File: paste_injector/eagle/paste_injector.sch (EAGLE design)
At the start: 20 parts, among them IC1 ULN2003AD, J2 USB, J5 PINHD-2X3, Q2 CSTCR6M00G53Z, U2 FT232RL, U4 ATMEGA328TQFP32

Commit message: Work in progress.
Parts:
- removed C5, C6, C7: 0.1uF, paste_injector:CAP-C0603
- removed U$28: OSH, paste_injector:OSH
- removed U2: FT232RL, paste_injector:FT232RL
- added C1: 0.1uF, paste_injector:CAP-C0603
- added JP2: (no value), paste_injector:PINHD-1X6
- R10, R2: value 10K -> 5K
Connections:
- removed net N$11: C6.1, U2.DTRO
- removed net N$16: C7.1, U2.3V3OUT
- removed net SER_RX: U2.TXO, U4.PD0(RXD)
- removed net SER_TX: U2.RXI, U4.PD1(TXD)
- removed net USB_DM: J2.D-, U2.D-
- removed net USB_DP: J2.D+, U2.D+
- new net DTR: C1.2, JP2.6
- new net RXI: JP2.4, U4.PD0(RXD)
- new net TXO: JP2.5, U4.PD1(TXD)
- net +5V: now also JP2.3; no longer C5.1, U2.VCC, U2.VCCIO
- net GND: now also JP2.1, JP2.2; no longer C5.2, C7.2, U2.GND@1, U2.GND@2, U2.GND@3, U2.GND@4, U2.TEST
- net RESET: now also C1.1; no longer C6.2
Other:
- note added: "0"
- note added: "FTDI BASIC"
- note added: "STATUS: EARLY DRAFT, DESIGN NOT VERIFIED YET."
- note removed: "1"
- note removed: "Serial (optional for debugging)"
- note removed: "TODO: add leds"
- moved on the sheet: C3, IC1, J5, JP1

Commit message: Minor tweaks.
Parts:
- removed JP2: (no value), paste_injector:PINHD-1X6
- removed LED1: (no value), arm-pro-mini-tester:LED
- added D1: (no value), paste_injector:LED
- added J1: USB, paste_injector:USB
- C1: value 0.1uF -> 10uF; device paste_injector:CAP-C0603 -> paste_injector:CPOL-USA/3216-18R
- C3: value 10uF -> 0.1uF; device paste_injector:CPOL-USA/3216-18R -> paste_injector:CAP-C0603
- J2: value USB -> (none); device paste_injector:USB -> paste_injector:PINHD-1X6
- R1: value (none) -> 10K; device paste_injector:TRIM_US-CA9V -> paste_injector:TRIMPOTCA9V
- renumbered C10 to C4, IC1 to U2, J5 to ISP, JP1 to J3, Q2 to Q1, R10 to R3, U4 to U1
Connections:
- net +5V: now also C1.+, J1.VBUS, J2.3, R1.CW; no longer C3.+, J2.VBUS, JP2.3, R1.E
- net BACKWARD: now also S2.2; no longer S1.2
- net DTR: now also C3.2, J2.6; no longer C1.2, JP2.6
- net FORWARD: now also S1.2; no longer S2.2
- net GND: now also C1.-, D1.C, J1.GND, J2.1, J2.2, R1.CCW, S1.GND, S2.GND; no longer C3.-, J2.GND, JP2.1, JP2.2, LED1.C, R1.A
- net M1: now also U1.PD2(INT0); no longer U1.PC2(ADC2)
- net M2: now also U1.PD3(INT1); no longer U1.PC3(ADC3)
- net M3: now also U1.PD4(XCK/T0); no longer U1.ADC6
- net M4: now also U1.PD5(T1); no longer U1.ADC7
- net N$1: now also D1.A; no longer LED1.A
- net POT: now also R1.C; no longer R1.S
- net RESET: now also C3.1; no longer C1.1
- net RXI: now also J2.4; no longer JP2.4
- net TXO: now also J2.5; no longer JP2.5
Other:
- note added: "+5V"
- note added: "CTS"
- note added: "DTR"
- note added: "GND"
- note added: "RXI"
- note added: "STATUS: NON VERIFIED DRAFT."
- note added: "TXO"
- note removed: "STATUS: EARLY DRAFT, DESIGN NOT VERIFIED YET."
- note removed: "TODO: pick potentiometer"
- note removed: "TODO: pick push buttons"
- moved on the sheet: C2

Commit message: Performed final routing.
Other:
- note added: "PUSH SPEED"
- note removed: "SPEED"
- moved on the sheet: J1
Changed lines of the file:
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@@
 <text x="172.72" y="68.58" size="3.048" layer="97">ISP</text>
 <text x="2.54" y="154.94" size="3.048" layer="97">POWER</text>
-<text x="15.24" y="96.52" size="3.048" layer="97">SPEED</text>
+<text x="15.24" y="96.52" size="3.048" layer="97">PUSH SPEED</text>
 <text x="96.52" y="71.12" size="3.048" layer="97">MOTOR DRIVER</text>
 <text x="200.66" y="116.84" size="3.048" layer="97">MCU</text>

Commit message: Saving open files.
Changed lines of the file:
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@@
 <part name="U$7" library="paste_injector" deviceset="NC" device=""/>
 <part name="R1" library="paste_injector" deviceset="TRIMPOT" device="CA9V" value="10K"/>
+<part name="U$8" library="paste_injector" deviceset="NC" device=""/>
+<part name="U$10" library="paste_injector" deviceset="NC" device=""/>
+<part name="U$11" library="paste_injector" deviceset="NC" device=""/>
+<part name="U$12" library="paste_injector" deviceset="NC" device=""/>
 </parts>
 <sheets>
@@
 <instance part="U$7" gate="G$1" x="231.14" y="177.8" rot="R180"/>
 <instance part="R1" gate="G$1" x="2.54" y="111.76"/>
+<instance part="U$8" gate="G$1" x="182.88" y="182.88" rot="R180"/>
+<instance part="U$10" gate="G$1" x="106.68" y="104.14" rot="R180"/>
+<instance part="U$11" gate="G$1" x="106.68" y="101.6" rot="R180"/>
+<instance part="U$12" gate="G$1" x="106.68" y="99.06" rot="R180"/>
 </instances>
 <busses>

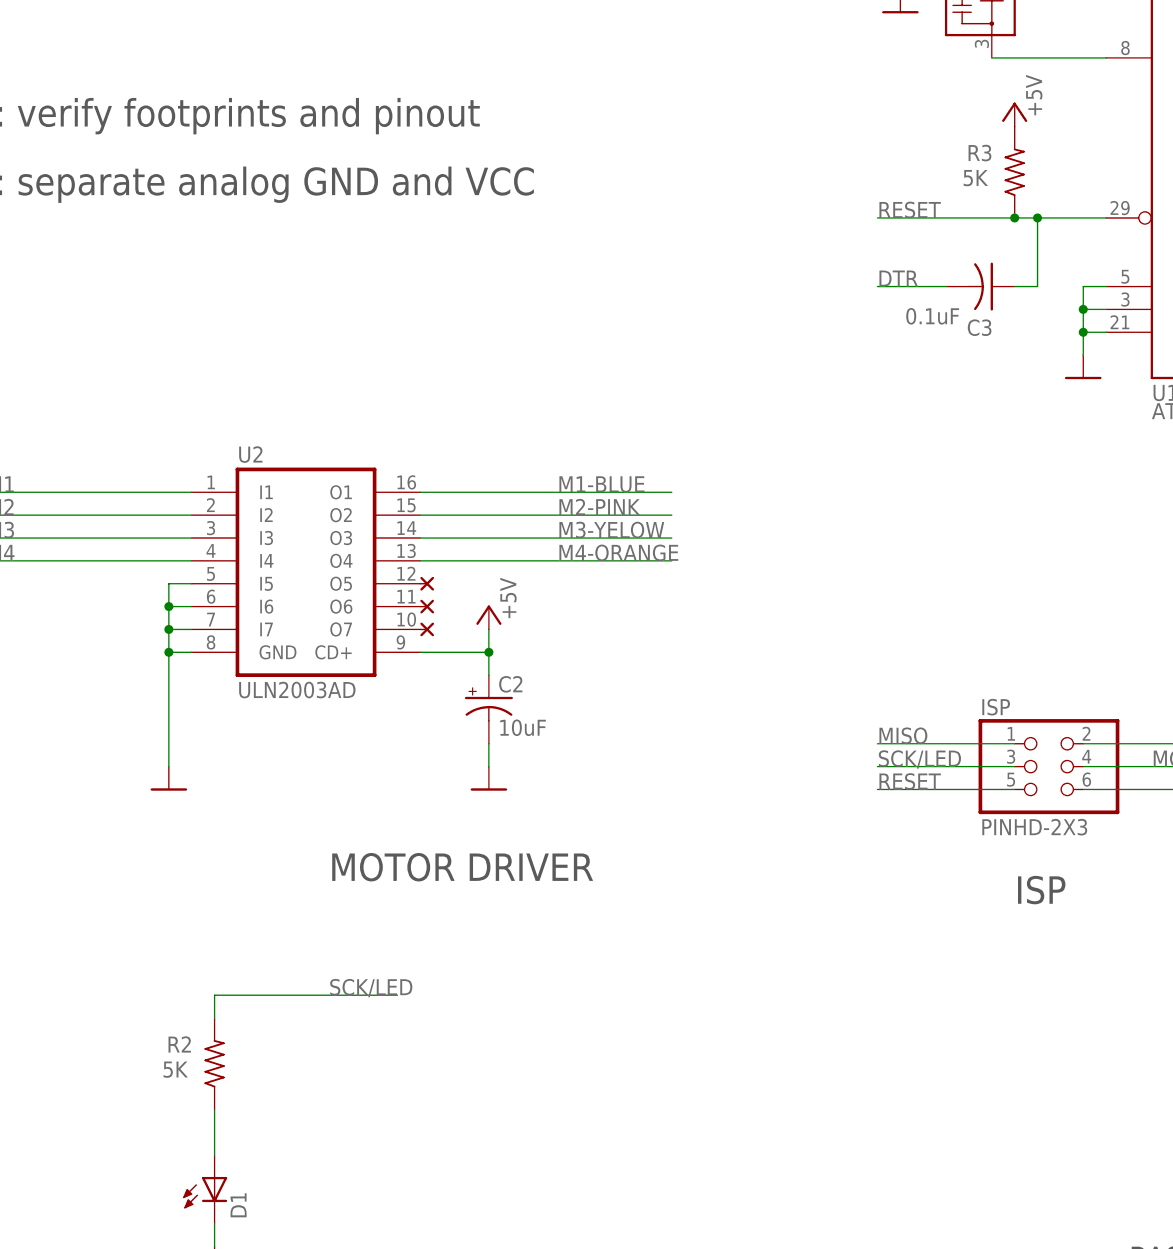
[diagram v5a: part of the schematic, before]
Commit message: Added BOM and TODO. Also, minor tweaks.
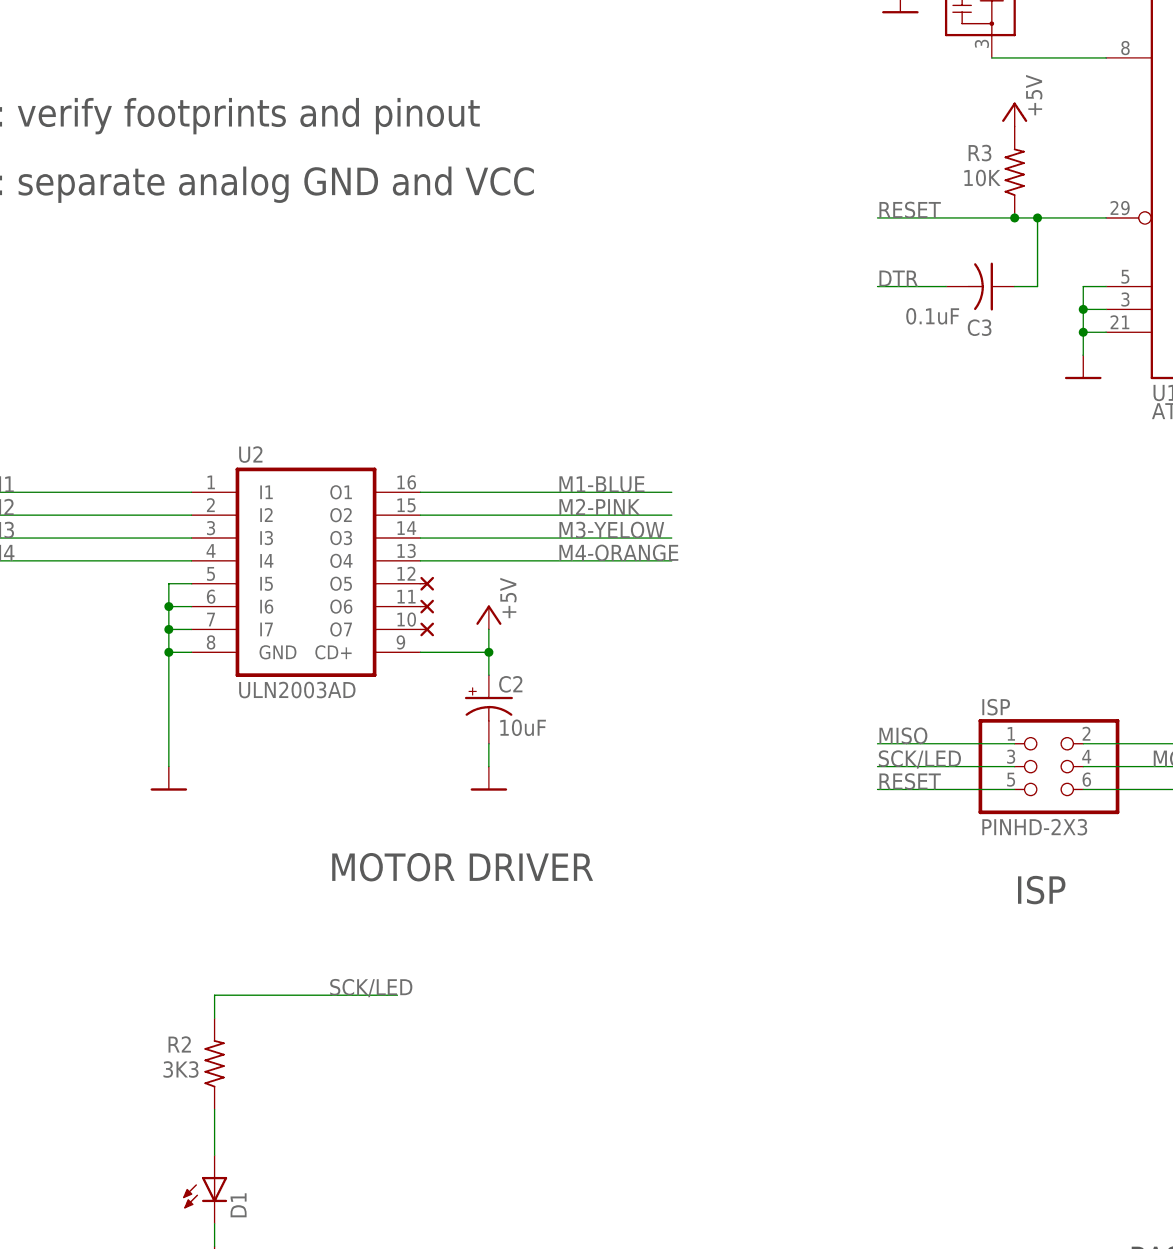
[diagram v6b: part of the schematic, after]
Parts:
- R2: value 5K -> 3K3
- R3: value 5K -> 10K
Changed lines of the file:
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@@
 <part name="GND14" library="paste_injector" deviceset="GND" device=""/>
 <part name="GND8" library="paste_injector" deviceset="GND" device=""/>
-<part name="R3" library="paste_injector" deviceset="RES-" device="R0603" value="5K"/>
+<part name="R3" library="paste_injector" deviceset="RES-" device="R0603" value="10K"/>
 <part name="C4" library="paste_injector" deviceset="CAP-" device="C0603" value="0.1uF"/>
 <part name="C1" library="paste_injector" deviceset="CPOL-US" device="A/3216-18R" value="10uF"/>
@@
 <part name="Q1" library="paste_injector" deviceset="CSTCR" device="" technology="6M00G53Z"/>
 <part name="D1" library="paste_injector" deviceset="LED" device=""/>
-<part name="R2" library="paste_injector" deviceset="RES-" device="R0603" value="5K"/>
+<part name="R2" library="paste_injector" deviceset="RES-" device="R0603" value="3K3"/>
 <part name="GND3" library="paste_injector" deviceset="GND" device=""/>
 <part name="P+8" library="paste_injector" deviceset="+5V" device=""/>

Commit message: Changed the board placement and rerouted (moved USB connector up) and push butto to the center.
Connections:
- net BACKWARD renamed PUSH
- net FORWARD renamed PULL
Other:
- note added: "1"
- note added: "FTDI BASIC HEADER"
- note added: "MOTOR PADS"
- note added: "POWER (USB)"
- note added: "PUSH-BUTTONS"
- note added: "SPEED"
- note added: "STATUS LED"
- note removed: "0"
- note removed: "FTDI BASIC"
- note removed: "MOTOR"
- note removed: "POWER"
- note removed: "PUSH SPEED"
- note removed: "STATUS: NON VERIFIED DRAFT."
- note removed: "TODO: separate analog GND and VCC"
- note removed: "TODO: verify footprints and pinout"
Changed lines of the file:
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@@
 <wire x1="281.94" y1="0" x2="-35.56" y2="0" width="0.1524" layer="94"/>
 <wire x1="-35.56" y1="0" x2="-35.56" y2="238.76" width="0.1524" layer="94"/>
-<text x="273.558" y="7.112" size="2.54" layer="97">0</text>
-<text x="48.26" y="154.94" size="3.048" layer="97">TODO: verify footprints and pinout</text>
+<text x="273.558" y="7.112" size="2.54" layer="97">1</text>
 <text x="172.72" y="68.58" size="3.048" layer="97">ISP</text>
-<text x="2.54" y="154.94" size="3.048" layer="97">POWER</text>
-<text x="15.24" y="96.52" size="3.048" layer="97">PUSH SPEED</text>
-<text x="96.52" y="71.12" size="3.048" layer="97">MOTOR DRIVER</text>
+<text x="2.54" y="154.94" size="3.048" layer="97">POWER (USB)</text>
+<text x="15.24" y="96.52" size="3.048" layer="97">SPEED</text>
+<text x="78.74" y="71.12" size="3.048" layer="97">MOTOR DRIVER</text>
 <text x="200.66" y="116.84" size="3.048" layer="97">MCU</text>
-<text x="48.26" y="147.32" size="3.048" layer="97">TODO: separate analog GND and VCC</text>
-<text x="231.14" y="71.12" size="3.048" layer="97">MOTOR</text>
+<text x="231.14" y="71.12" size="3.048" layer="97">MOTOR PADS</text>
 <text x="233.68" y="185.166" size="1.524" layer="97">(open col.)</text>
-<text x="81.28" y="175.26" size="3.048" layer="97">FTDI BASIC</text>
-<text x="2.54" y="220.98" size="5.08" layer="97">STATUS: NON VERIFIED DRAFT.</text>
+<text x="66.04" y="175.26" size="3.048" layer="97">FTDI BASIC HEADER</text>
 <text x="106.934" y="187.198" size="1.778" layer="98">DTR</text>
 <text x="106.934" y="189.738" size="1.778" layer="98">TXO</text>
@@
 <text x="106.934" y="199.898" size="1.778" layer="132">GND</text>
 <text x="233.68" y="182.626" size="1.524" layer="97">(open col.)</text>
+<text x="78.74" y="17.78" size="3.048" layer="97">STATUS LED</text>
+<text x="-2.54" y="17.78" size="3.048" layer="97">PUSH-BUTTONS</text>
 </plain>
 <instances>
@@
 </segment>
 </net>
-<net name="FORWARD" class="0">
+<net name="PULL" class="0">
 <segment>
 <pinref part="U1" gate="G$1" pin="PD6(AIN0)"/>
@@
 <pinref part="S1" gate="G$1" pin="2"/>
 <wire x1="0" y1="45.72" x2="0" y2="58.42" width="0.1524" layer="91"/>
-<wire x1="0" y1="58.42" x2="40.64" y2="58.42" width="0.1524" layer="91"/>
-<label x="22.86" y="55.88" size="1.778" layer="95"/>
-</segment>
-</net>
-<net name="BACKWARD" class="0">
+<wire x1="0" y1="58.42" x2="35.56" y2="58.42" width="0.1524" layer="91"/>
+<label x="27.94" y="58.42" size="1.778" layer="95"/>
+</segment>
+</net>
+<net name="PUSH" class="0">
 <segment>
 <pinref part="U1" gate="G$1" pin="PD7(AIN1)"/>
@@
 <pinref part="S2" gate="G$1" pin="2"/>
 <wire x1="15.24" y1="45.72" x2="15.24" y2="50.8" width="0.1524" layer="91"/>
-<wire x1="15.24" y1="50.8" x2="40.64" y2="50.8" width="0.1524" layer="91"/>
-<label x="22.86" y="50.8" size="1.778" layer="95"/>
-</segment>
-</net>
+<wire x1="15.24" y1="50.8" x2="35.56" y2="50.8" width="0.1524" layer="91"/>
+<label x="27.94" y="50.8" size="1.778" layer="95"/>
+</segment>
+</net>

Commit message: Tweaked the design, updated the BOM.
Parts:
- removed C2: 10uF, paste_injector:CPOL-USA/3216-18R
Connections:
- net +5V: no longer C2.+
- net GND: no longer C2.-
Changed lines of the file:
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@@
 <part name="P+4" library="paste_injector" deviceset="+5V" device=""/>
 <part name="P+5" library="paste_injector" deviceset="+5V" device=""/>
-<part name="C2" library="paste_injector" deviceset="CPOL-US" device="A/3216-18R" value="10uF"/>
-<part name="GND4" library="paste_injector" deviceset="GND" device=""/>
 <part name="GND17" library="paste_injector" deviceset="GND" device=""/>
 <part name="P+7" library="paste_injector" deviceset="+5V" device=""/>
@@
 <attribute name="VALUE" x="198.628" y="89.916" size="1.778" layer="96" rot="R90"/>
 </instance>
-<instance part="C2" gate="G$1" x="114.3" y="91.44"/>
-<instance part="GND4" gate="1" x="114.3" y="81.28"/>
 <instance part="GND17" gate="1" x="2.54" y="99.06"/>
 <instance part="P+7" gate="1" x="2.54" y="124.46" smashed="yes">
@@
 </segment>
 <segment>
-<pinref part="C2" gate="G$1" pin="-"/>
-<pinref part="GND4" gate="1" pin="GND"/>
-<wire x1="114.3" y1="86.36" x2="114.3" y2="83.82" width="0.1524" layer="91"/>
-</segment>
-<segment>
 <pinref part="GND17" gate="1" pin="GND"/>
 <wire x1="2.54" y1="104.14" x2="2.54" y2="101.6" width="0.1524" layer="91"/>
@@
 <wire x1="114.3" y1="96.52" x2="114.3" y2="99.06" width="0.1524" layer="91"/>
 <pinref part="P+2" gate="1" pin="+5V"/>
-<pinref part="C2" gate="G$1" pin="+"/>
-<wire x1="114.3" y1="93.98" x2="114.3" y2="96.52" width="0.1524" layer="91"/>
-<junction x="114.3" y="96.52"/>
-</segment>
-<segment>
+</segment>
+<segment>
